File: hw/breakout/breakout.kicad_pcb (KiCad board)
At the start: 2 copper layers, 50.8 x 58.4 mm, 46 parts, among them J1 Rain, J10 SPI_CS, J11 Uart, J12 GPS, J13 RX_SEL, J2 Wind, J3 ARM-SWD, J4 PWR_IN, J5 PWR, J6 GPIO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

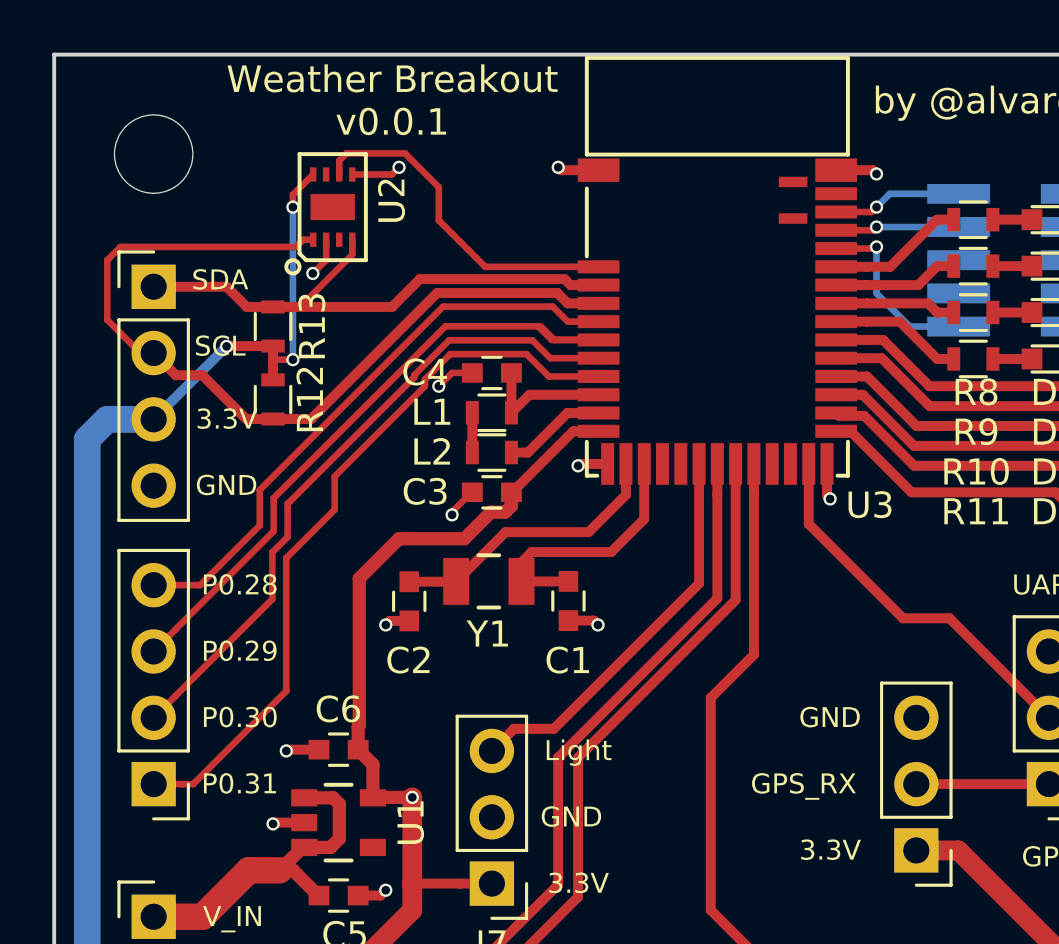
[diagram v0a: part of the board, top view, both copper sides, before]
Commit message: Updated MDBT42Q footprint and layout
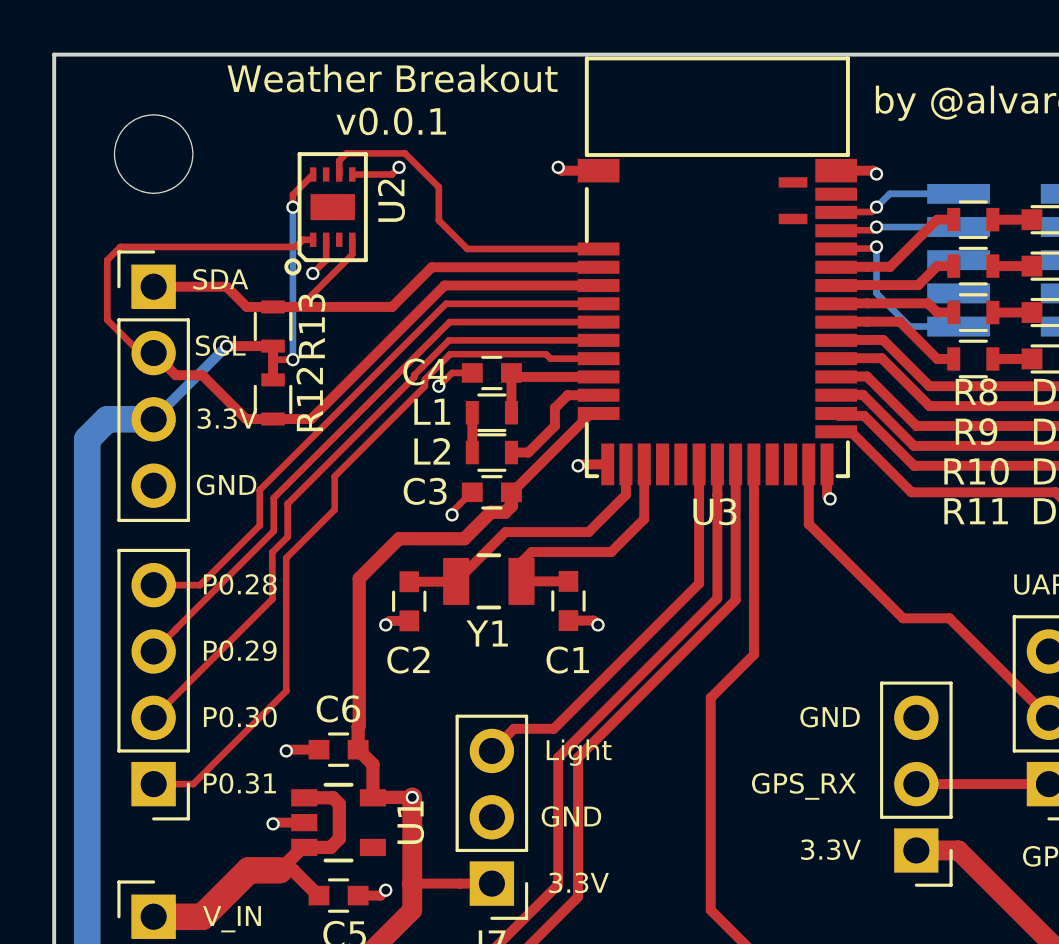
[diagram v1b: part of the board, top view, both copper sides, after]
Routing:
- net /P0.29: track 25.6 -> 23.0 mm
- net Net-(L2-Pad2): track 3.96 -> 4.65 mm

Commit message: Update version on schematic
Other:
- rule pad_to_mask_clearance: 0.127 -> 0.0508
- board text added: "Weather Breakout v0.0.2"
- board text removed: "Weather Breakout v0.0.1"
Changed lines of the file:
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@@
-(kicad_pcb (version 4) (host pcbnew 4.0.7-e2-6376~58~ubuntu16.04.1)
+(kicad_pcb (version 4) (host pcbnew 4.0.7)
   (general
     (links 98)
     (no_connects 0)
-    (area 126.924999 68.504999 177.875001 127.075001)
+    (area 123.443314 66.5976 181.356686 128.607401)
     (thickness 1.6)
     (drawings 47)
@@
   )
   (page A4)
+  (title_block
+    (title "Weather Breakout")
+    (date 2018-01-01)
+    (rev 0.0.2)
+    (company @alvaroprieto)
+  )
   (layers
     (0 F.Cu signal)
@@
   )
   (setup
-    (last_trace_width 0.254)
+    (last_trace_width 0.1524)
     (user_trace_width 0.1524)
     (user_trace_width 0.254)
@@
     (pad_size 1.524 1.524)
     (pad_drill 0.762)
-    (pad_to_mask_clearance 0.127)
+    (pad_to_mask_clearance 0.0508)
     (aux_axis_origin 0 0)
     (visible_elements FFFFFF7F)
@@
     (effects (font (size 1.016 1.016) (thickness 0.1778)))
   )
-  (gr_text "Weather Breakout\nv0.0.1" (at 139.954 70.358) (layer F.SilkS)
+  (gr_text "Weather Breakout\nv0.0.2" (at 139.954 70.358) (layer F.SilkS)
     (effects (font (size 1.016 1.016) (thickness 0.1778)))
   )
